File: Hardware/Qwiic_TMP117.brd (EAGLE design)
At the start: 22.9 x 24.1 mm, 42 parts, among them J1 PTH, U1 TMP117

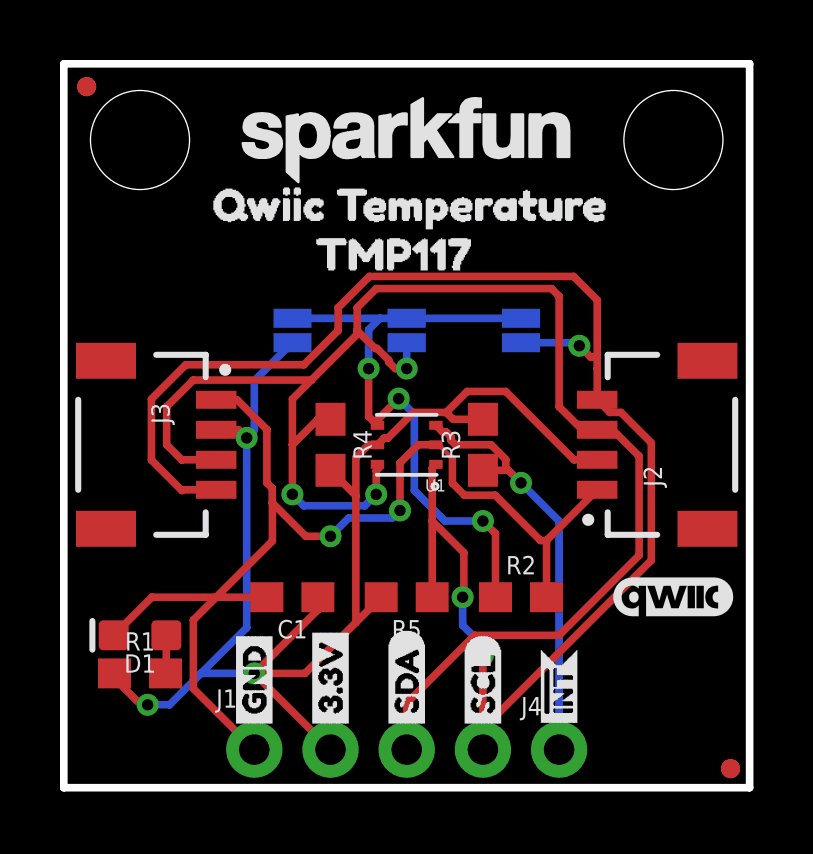
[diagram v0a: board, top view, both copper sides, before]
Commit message: Updated Schematic and Boar
Fixed the board with the polygon and added a table to the schematic describing the pin addresses for ADD0
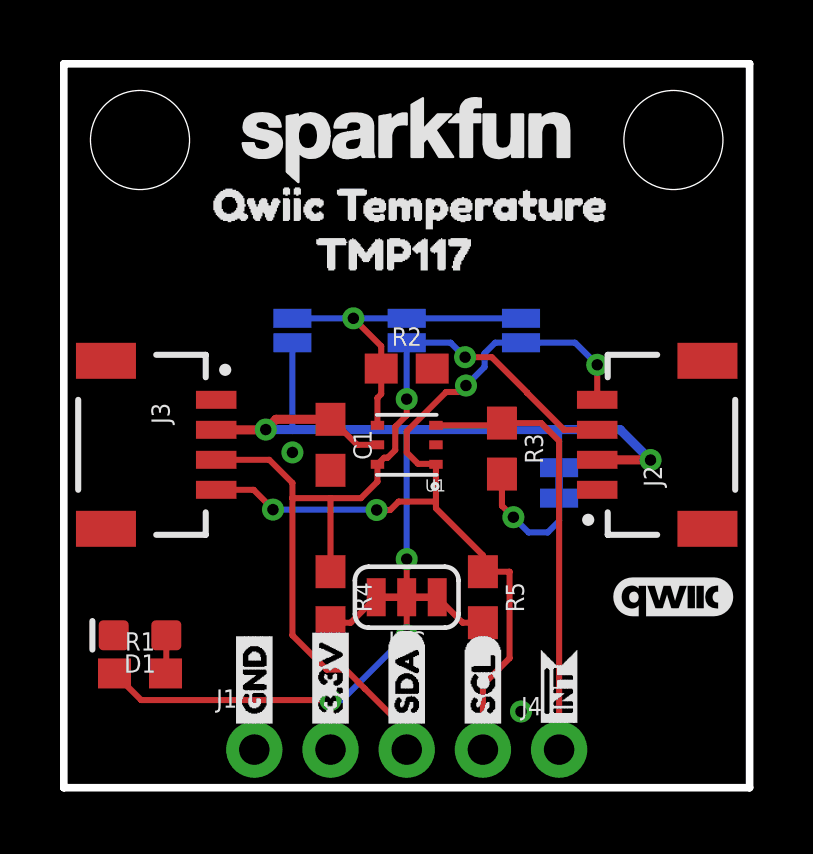
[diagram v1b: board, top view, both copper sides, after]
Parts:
- removed JP4, JP5, JP6, JP7: FIDUCIALUFIDUCIAL, SparkFun:MICRO-FIDUCIAL
- added I2C: (no value), SparkFun-Jumpers:SMT-JUMPER_3_2-NC_TRACE_SILK
- added JP10: INT, SparkFun-Passives:PAD-JUMPER-2-NC_BY_TRACE_YES_SILK
- JP1, JP2, JP3: value JUMPER-SMT_2_NO_SILK -> (none)
- R3: value 2.2k -> 10k
- moved R2 8.52 mm to (11.4, 14.0)
- moved C1 5.24 mm to (8.89, 11.4), turned to 270 degrees
- moved R4 5.08 mm to (8.89, 6.35)
- moved R5 2.54 mm to (14.0, 6.35), turned to 270 degrees
- moved R3 0.65 mm to (14.6, 11.3), turned to 270 degrees
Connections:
- new net N$2: I2C.1, R5.2
- new net N$3: I2C.3, R4.2
- new net N$4: JP10.1, R3.2
- net 3.3V: now also I2C.2, JP10.2; no longer R3.2, R4.2, R5.2
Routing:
- net GND: track 38.4 -> 0.00 mm
- net SCL: track 55.1 -> 30.3 mm, vias 3 -> 4
- net SDA: track 53.1 -> 31.9 mm, vias 3 -> 2
- net ADD0: track 21.3 -> 11.6 mm, vias 3 -> 1
- net 3.3V: track 49.2 -> 44.6 mm, vias 3 -> 5
- net N$4: track 0.00 -> 4.25 mm, vias 0 -> 1
- net N$2: track 0.00 -> 1.88 mm
- net N$3: track 0.00 -> 1.88 mm
- net !INT: track 14.1 -> 14.9 mm, vias 1 -> 0
- added copper zone on layer 16, net GND

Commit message: Updated PCB
Fixed the board to meet the specifications for the data sheet's PCB considerations
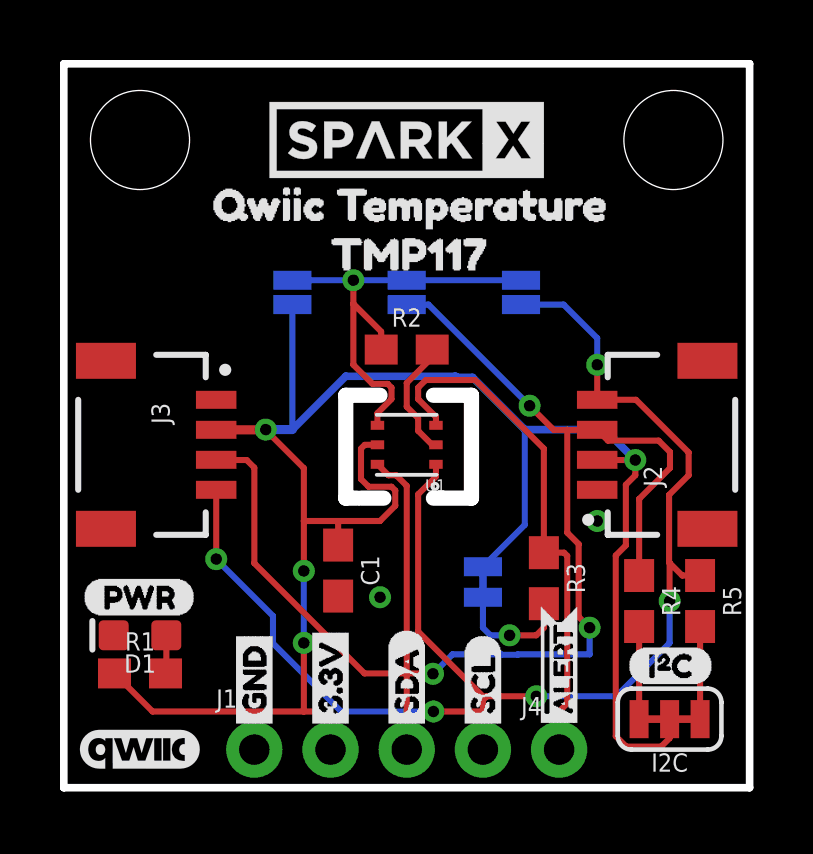
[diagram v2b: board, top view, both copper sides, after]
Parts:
- removed U$1: SFE_LOGO_NAME.1_INCH, SparkFun-Aesthetics:SFE_LOGO_NAME_.1
- added U$20: (no value), buzzard_labels (10):#ALERT0
- added U$21: (no value), Labels:PWR-()-03
- U$17: device Labels-0_04:(I_SUPER2_C) -> SparkX:SPARKX-MEDIUM
- U$19: device buzzard_labels (5):#INT8 -> Labels:I_SUPER2_C-()-03
- U$2: value SFE_LOGO_NAME_FLAME.1_INCH -> (none); device SparkFun-Aesthetics:SFE_LOGO_NAME_FLAME_.1 -> SparkX:SPARKX-MEDIUM
- U$7: device buzzard_labels (5):#INT8 -> buzzard_labels (10):#ALERT0
- moved U$3 18.5 mm to (2.54, 1.27)
- moved R4 10.3 mm to (19.2, 6.22)
- moved I2C 9.66 mm to (20.2, 2.29)
- moved R5 7.24 mm to (21.2, 6.22)
- moved R3 4.54 mm to (16.0, 6.99)
- moved C1 4.20 mm to (9.14, 7.24)
- moved JP10 4.17 mm to (14.0, 6.86)
- moved U$17 4.15 mm to (11.4, 21.6), flipped to the top
- moved U$19 3.32 mm to (18.8, 4.06), flipped to the top, turned to 0 degrees
- moved JP1 1.27 mm to (15.2, 16.5)
- moved JP2 1.27 mm to (11.4, 16.5)
- moved JP3 1.27 mm to (7.62, 16.5)
- moved U$18 1.27 mm to (13.2, 14.6)
- moved U$5 1.27 mm to (9.40, 14.6)
- moved U$8 1.27 mm to (16.9, 14.6)
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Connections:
- net !INT renamed !ALERT
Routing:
- net 3.3V: track 44.6 -> 64.7 mm, vias 5 -> 4
- net SDA: track 31.9 -> 50.8 mm, vias 2 -> 3
- net SCL: track 30.3 -> 48.2 mm, vias 4 -> 5
- net GND: track 0.00 -> 4.01 mm
- net ADD0: track 11.6 -> 15.4 mm
- net !ALERT: track 14.9 -> 17.6 mm
- net N$3: track 1.88 -> 3.09 mm
- net N$2: track 1.88 -> 3.09 mm
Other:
- outline, holes or cut-outs redrawn

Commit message: Updated Board
Fixed wiring and polygons
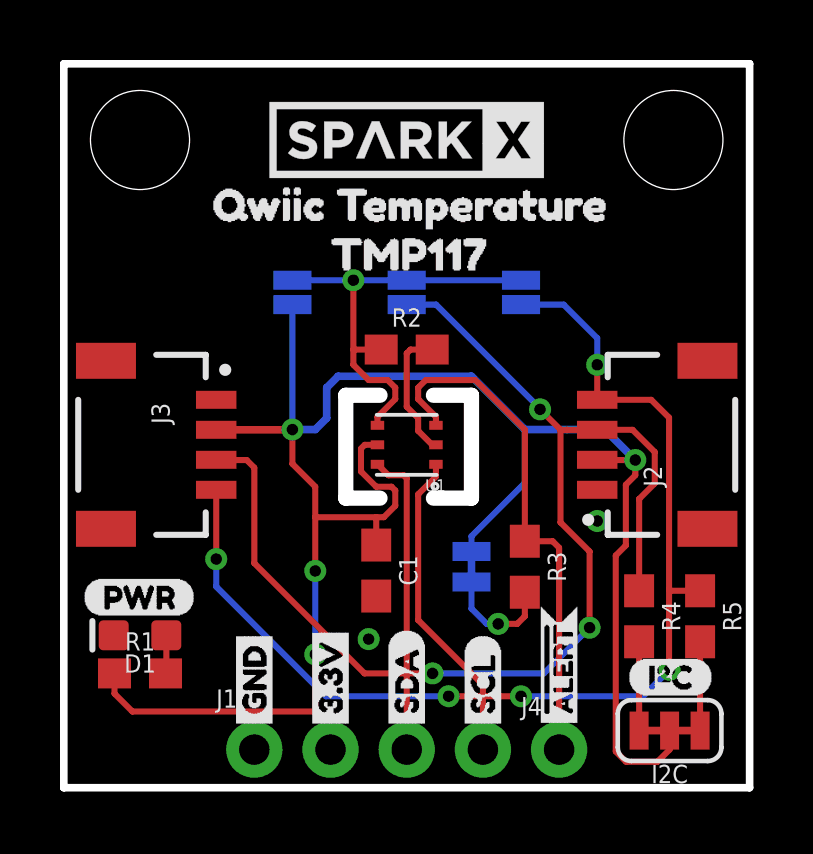
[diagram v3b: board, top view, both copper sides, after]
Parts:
- removed U$3: QWIIC_LOGO_4MM, SparkFun-Aesthetics:QWIIC_4MM
- added U$1: (no value), buzzard_labels (11):ADD0_JUMPERS0
- moved C1 1.27 mm to (10.4, 7.24)
- moved U$2 1.27 mm to (11.4, 21.6)
- moved R3 0.74 mm to (15.4, 7.37)
- moved JP10 0.64 mm to (13.6, 7.37)
- moved R4 0.51 mm to (19.2, 5.71)
- moved R5 0.51 mm to (21.2, 5.71)
- moved U$19 0.38 mm to (18.8, 3.68)
- moved I2C 0.38 mm to (20.2, 1.91)
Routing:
- net ADD0: track 15.4 -> 14.6 mm
- net 3.3V: track 64.7 -> 65.3 mm
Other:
- outline, holes or cut-outs redrawn
